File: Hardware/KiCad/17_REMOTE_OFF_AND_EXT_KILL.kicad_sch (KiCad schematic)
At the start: 0 parts

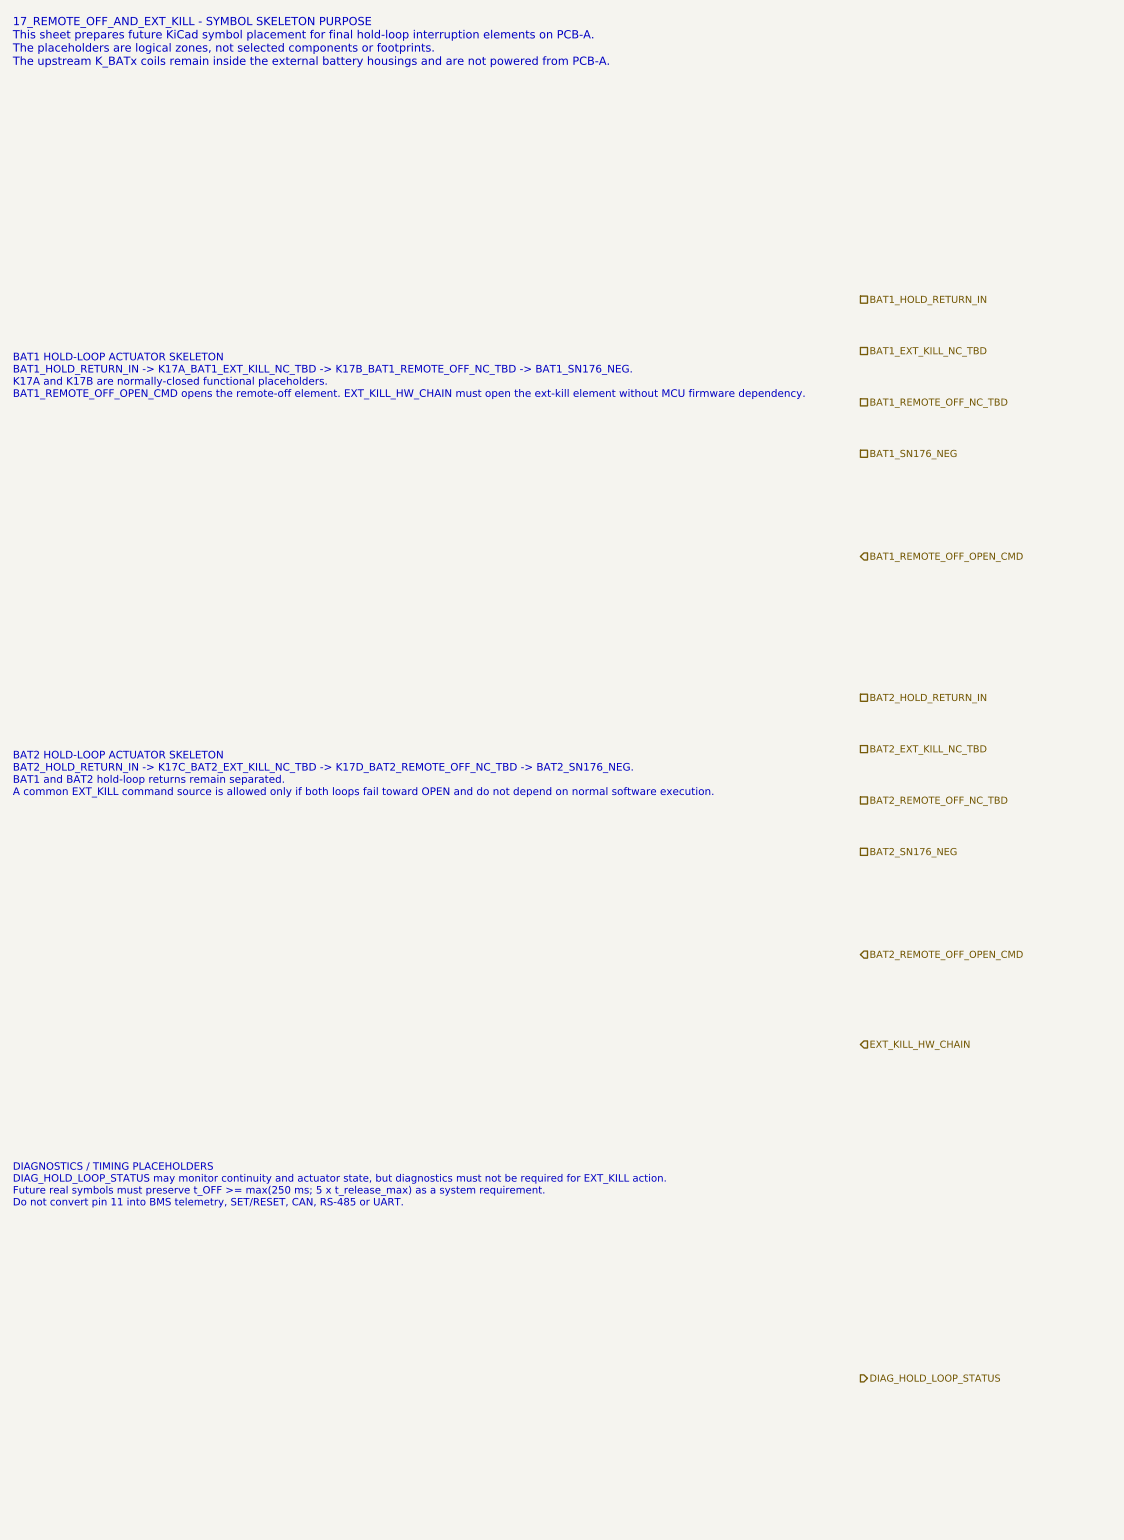
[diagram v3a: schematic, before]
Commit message: hardware: align PCB-B CTRL_RESERVE interfaces
Merge PCB-B interface consistency fixes after verifying canonical names, diagnostics, and independent EXT_KILL final actions.
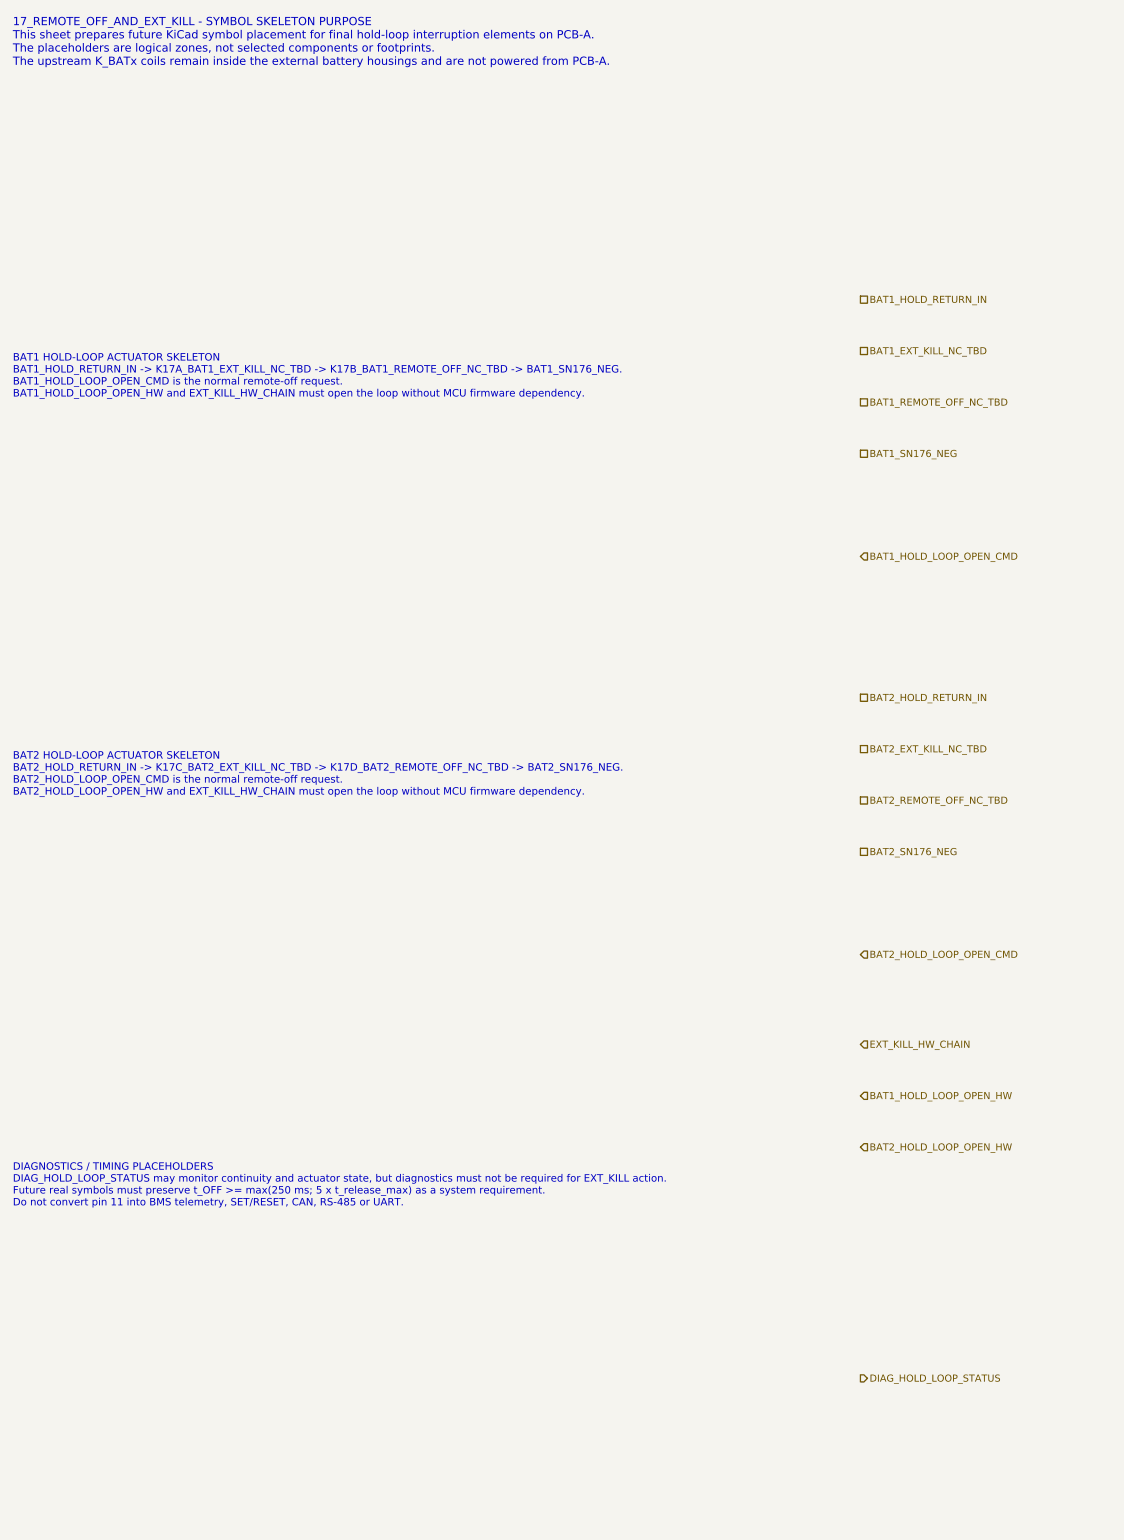
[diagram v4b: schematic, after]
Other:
- note added: "BAT1 HOLD-LOOP ACTUATOR SKELETON BAT1_HOLD_RETURN_IN -> K17A_BAT1_EXT_KILL_NC_TBD -> K17B_BAT1_REMOTE_OFF_NC_TBD -> BAT1_SN176_NEG. BAT1_HOLD_LOOP_OPEN_CMD is the normal remote-off request. BAT1_HOLD_LOOP_OPEN_HW and EXT_KILL_HW_CHAIN must open the loop without MCU firmware dependency."
- note added: "BAT2 HOLD-LOOP ACTUATOR SKELETON BAT2_HOLD_RETURN_IN -> K17C_BAT2_EXT_KILL_NC_TBD -> K17D_BAT2_REMOTE_OFF_NC_TBD -> BAT2_SN176_NEG. BAT2_HOLD_LOOP_OPEN_CMD is the normal remote-off request. BAT2_HOLD_LOOP_OPEN_HW and EXT_KILL_HW_CHAIN must open the loop without MCU firmware dependency."
- note removed: "BAT1 HOLD-LOOP ACTUATOR SKELETON BAT1_HOLD_RETURN_IN -> K17A_BAT1_EXT_KILL_NC_TBD -> K17B_BAT1_REMOTE_OFF_NC_TBD -> BAT1_SN176_NEG. K17A and K17B are normally-closed functional placeholders. BAT1_REMOTE_OFF_OPEN_CMD opens the remote-off element. EXT_KILL_HW_CHAIN must open the ext-kill element without MCU firmware dependency."
- note removed: "BAT2 HOLD-LOOP ACTUATOR SKELETON BAT2_HOLD_RETURN_IN -> K17C_BAT2_EXT_KILL_NC_TBD -> K17D_BAT2_REMOTE_OFF_NC_TBD -> BAT2_SN176_NEG. BAT1 and BAT2 hold-loop returns remain separated. A common EXT_KILL command source is allowed only if both loops fail toward OPEN and do not depend on normal software execution."
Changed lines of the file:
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@@
 		(title "17_REMOTE_OFF_AND_EXT_KILL - hold-loop final actuators")
 		(date "2026-07-15")
-		(rev "C1")
+		(rev "C2")
 		(company "Gonoboben/plataVM")
-		(comment 1 "Interface consistency: NC actuator zones and exact hold-loop return nets")
+		(comment 1 "Interface consistency: canonical hold-loop commands and branch-specific hardware-open actions")
 		(comment 2 "Text-only placeholders; no relay, MOSFET, optocoupler or driver topology selected")
 	)
@@
 		(uuid "bfe-symbol-00000017-0000-4000-8000-000000000101")
 	)
-	(text "BAT1 HOLD-LOOP ACTUATOR SKELETON\nBAT1_HOLD_RETURN_IN -> K17A_BAT1_EXT_KILL_NC_TBD -> K17B_BAT1_REMOTE_OFF_NC_TBD -> BAT1_SN176_NEG.\nK17A and K17B are normally-closed functional placeholders.\nBAT1_REMOTE_OFF_OPEN_CMD opens the remote-off element. EXT_KILL_HW_CHAIN must open the ext-kill element without MCU firmware dependency."
+	(text "BAT1 HOLD-LOOP ACTUATOR SKELETON\nBAT1_HOLD_RETURN_IN -> K17A_BAT1_EXT_KILL_NC_TBD -> K17B_BAT1_REMOTE_OFF_NC_TBD -> BAT1_SN176_NEG.\nBAT1_HOLD_LOOP_OPEN_CMD is the normal remote-off request.\nBAT1_HOLD_LOOP_OPEN_HW and EXT_KILL_HW_CHAIN must open the loop without MCU firmware dependency."
 		(exclude_from_sim no)
 		(at 12 66 0)
-		(effects (font (size 1.18 1.18)) (justify left))
+		(effects (font (size 1.16 1.16)) (justify left))
 		(uuid "bfe-symbol-00000017-0000-4000-8000-000000000102")
 	)
-	(text "BAT2 HOLD-LOOP ACTUATOR SKELETON\nBAT2_HOLD_RETURN_IN -> K17C_BAT2_EXT_KILL_NC_TBD -> K17D_BAT2_REMOTE_OFF_NC_TBD -> BAT2_SN176_NEG.\nBAT1 and BAT2 hold-loop returns remain separated.\nA common EXT_KILL command source is allowed only if both loops fail toward OPEN and do not depend on normal software execution."
+	(text "BAT2 HOLD-LOOP ACTUATOR SKELETON\nBAT2_HOLD_RETURN_IN -> K17C_BAT2_EXT_KILL_NC_TBD -> K17D_BAT2_REMOTE_OFF_NC_TBD -> BAT2_SN176_NEG.\nBAT2_HOLD_LOOP_OPEN_CMD is the normal remote-off request.\nBAT2_HOLD_LOOP_OPEN_HW and EXT_KILL_HW_CHAIN must open the loop without MCU firmware dependency."
 		(exclude_from_sim no)
 		(at 12 128 0)
-		(effects (font (size 1.18 1.18)) (justify left))
+		(effects (font (size 1.16 1.16)) (justify left))
 		(uuid "bfe-symbol-00000017-0000-4000-8000-000000000103")
 	)
@@
 	(hierarchical_label "BAT2_REMOTE_OFF_NC_TBD" (shape passive) (exclude_from_sim no) (at 144 132 0) (effects (font (size 1.1 1.1)) (justify left)) (uuid "bfe-symbol-00000017-0000-4000-8000-000000000207"))
 	(hierarchical_label "BAT2_SN176_NEG" (shape passive) (exclude_from_sim no) (at 144 140 0) (effects (font (size 1.1 1.1)) (justify left)) (uuid "bfe-symbol-00000017-0000-4000-8000-000000000208"))
-	(hierarchical_label "BAT1_REMOTE_OFF_OPEN_CMD" (shape input) (exclude_from_sim no) (at 144 94 0) (effects (font (size 1.1 1.1)) (justify left)) (uuid "bfe-symbol-00000017-0000-4000-8000-000000000209"))
-	(hierarchical_label "BAT2_REMOTE_OFF_OPEN_CMD" (shape input) (exclude_from_sim no) (at 144 156 0) (effects (font (size 1.1 1.1)) (justify left)) (uuid "bfe-symbol-00000017-0000-4000-8000-000000000210"))
+	(hierarchical_label "BAT1_HOLD_LOOP_OPEN_CMD" (shape input) (exclude_from_sim no) (at 144 94 0) (effects (font (size 1.1 1.1)) (justify left)) (uuid "bfe-symbol-00000017-0000-4000-8000-000000000209"))
+	(hierarchical_label "BAT2_HOLD_LOOP_OPEN_CMD" (shape input) (exclude_from_sim no) (at 144 156 0) (effects (font (size 1.1 1.1)) (justify left)) (uuid "bfe-symbol-00000017-0000-4000-8000-000000000210"))
 	(hierarchical_label "EXT_KILL_HW_CHAIN" (shape input) (exclude_from_sim no) (at 144 170 0) (effects (font (size 1.1 1.1)) (justify left)) (uuid "bfe-symbol-00000017-0000-4000-8000-000000000211"))
+	(hierarchical_label "BAT1_HOLD_LOOP_OPEN_HW" (shape input) (exclude_from_sim no) (at 144 178 0) (effects (font (size 1.1 1.1)) (justify left)) (uuid "bfe-symbol-00000017-0000-4000-8000-000000000213"))
+	(hierarchical_label "BAT2_HOLD_LOOP_OPEN_HW" (shape input) (exclude_from_sim no) (at 144 186 0) (effects (font (size 1.1 1.1)) (justify left)) (uuid "bfe-symbol-00000017-0000-4000-8000-000000000214"))
 	(hierarchical_label "DIAG_HOLD_LOOP_STATUS" (shape output) (exclude_from_sim no) (at 144 222 0) (effects (font (size 1.1 1.1)) (justify left)) (uuid "bfe-symbol-00000017-0000-4000-8000-000000000212"))
 )
